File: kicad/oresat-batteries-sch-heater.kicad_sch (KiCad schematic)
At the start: 22 parts, among them Q20 PMV45ENR, Q21 PMV45ENR, Q38 PMV45ENR, Q39 PMV45ENR, Q42 DMP2240UDM-7, Q43 DMP2240UDM-7

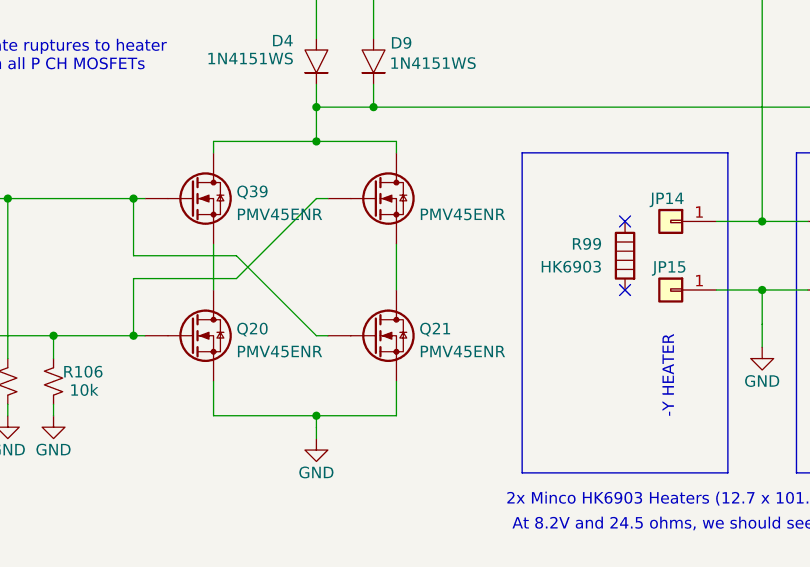
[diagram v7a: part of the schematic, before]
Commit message: Intermediary state on v4. Added one of two efuses.
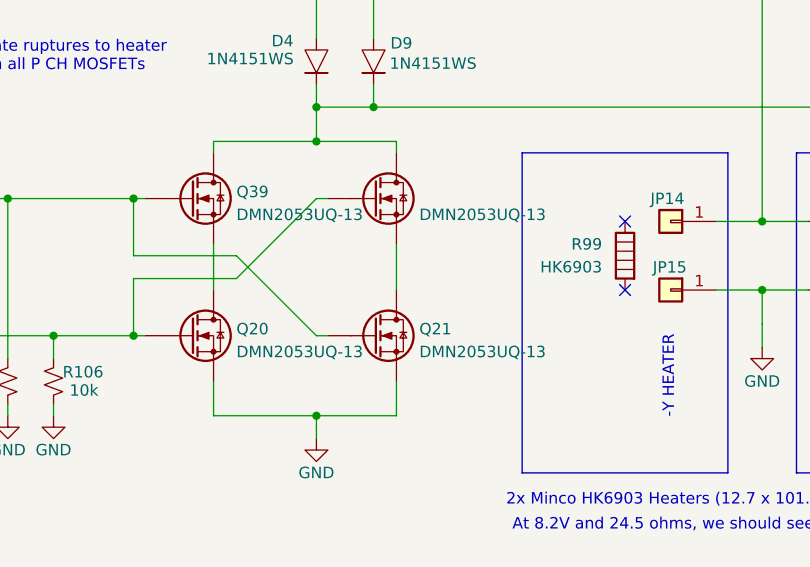
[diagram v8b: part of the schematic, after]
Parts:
- Q20, Q21, Q38, Q39: value PMV45ENR -> DMN2053UQ-13; DPN 1727-2307-1-ND -> 31-DMN2053UQ-13CT-ND; MFR Nexperia -> Diodes Incorporated; MPN PMV45EN2R -> DMN2053UQ-13
